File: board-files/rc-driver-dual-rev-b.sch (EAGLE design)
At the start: 20 parts

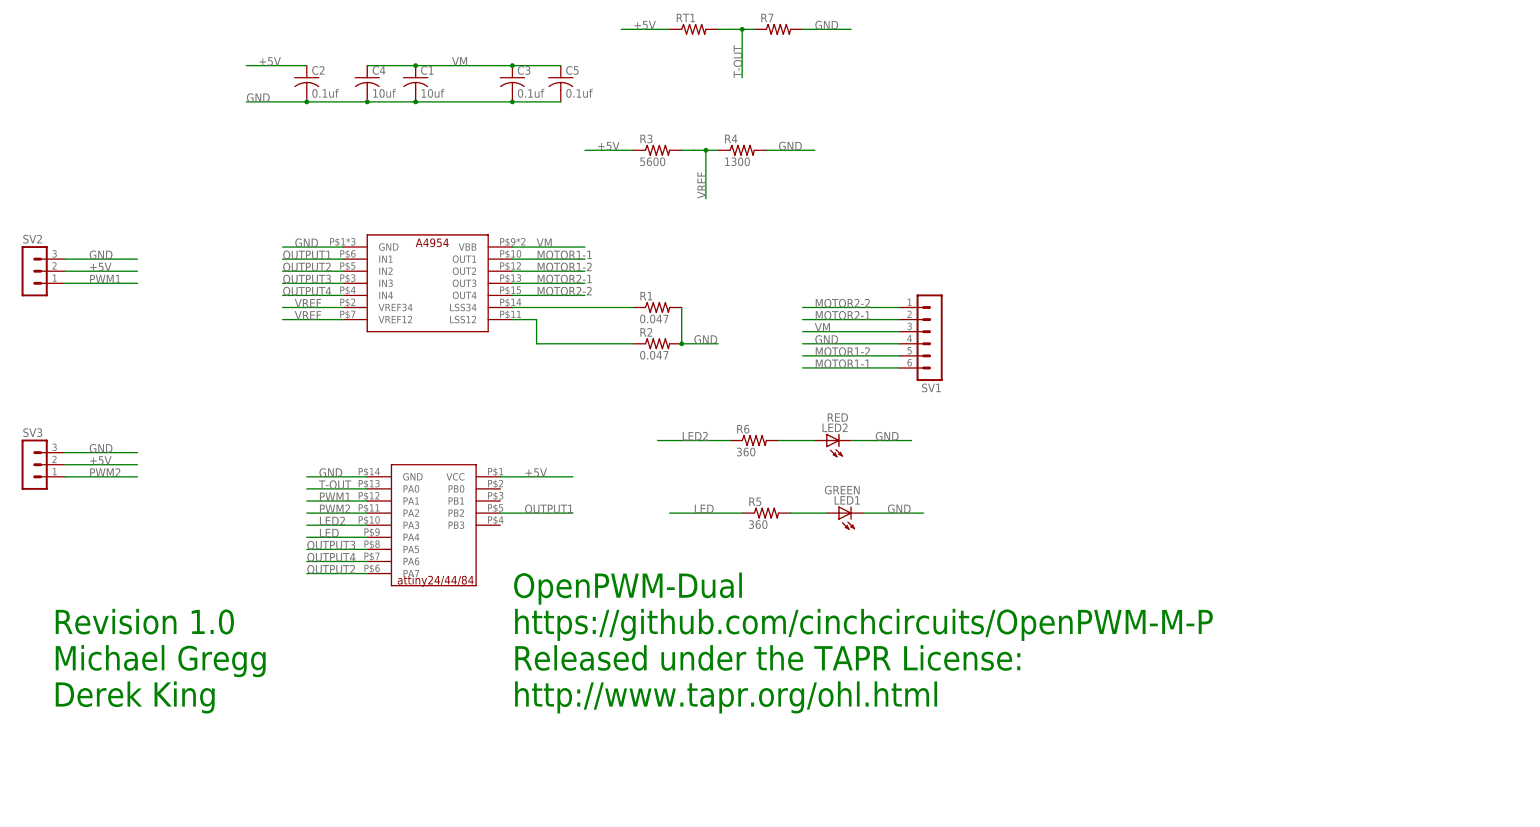
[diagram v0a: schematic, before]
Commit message: First pass layout of revB designed that include 5V regulator Improved part outlines in library.
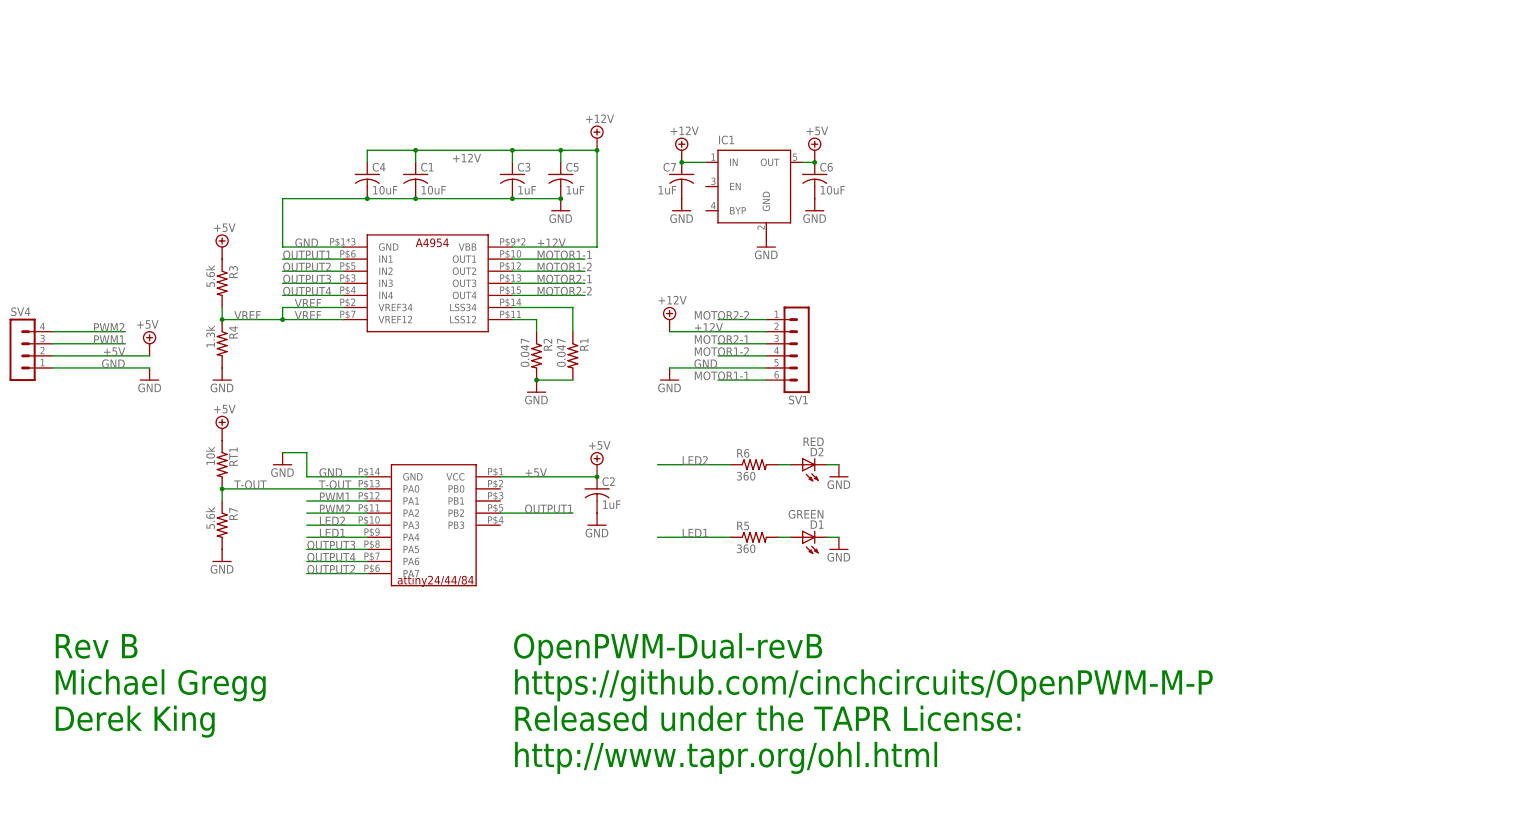
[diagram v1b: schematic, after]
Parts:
- removed LED1: GREEN, led:LEDCHIPLED_0603
- removed LED2: RED, led:LEDCHIPLED_0603
- removed SV2, SV3: (no value), con-lstb:MA03-1
- added C6: 10uF, resistor:C-USC1206
- added C7: 1uF, resistor:C-USC0603
- added D1: GREEN, led:LEDCHIPLED_0603
- added D2: RED, led:LEDCHIPLED_0603
- added IC1: (no value), v-reg-micrel:MIC5219XX
- added SV4: (no value), con-lstb:MA04-1
- C1, C4: value 10uf -> 10uF
- C2, C3, C5: value 0.1uf -> 1uF
- R1, R2: device resistor:R-US_R0805W -> resistor:R-US_R0805
- R3: value 5600 -> 5.6k
- R4: value 1300 -> 1.3k
- R7: value (none) -> 5.6k
- RT1: value (none) -> 10k
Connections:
- net LED renamed LED1
- removed net VM: C1.1, C3.1, C4.1, C5.1, SV1.3, U$2.VBB
- new net +12V: C1.1, C3.1, C4.1, C5.1, C7.1, IC1.IN, SV1.2, U$2.VBB
- net +5V: now also C6.1, IC1.OUT, SV4.2; no longer SV2.2, SV3.2
- net GND: now also C6.2, C7.2, D1.C, D2.C, IC1.GND, SV1.5, SV4.1; no longer LED1.C, LED2.C, SV1.4, SV2.3, SV3.3
- net MOTOR1-2: now also SV1.4; no longer SV1.5
- net MOTOR2-1: now also SV1.3; no longer SV1.2
- net N$3: now also D2.A; no longer LED2.A
- net N$4: now also D1.A; no longer LED1.A
- net PWM1: now also SV4.3; no longer SV2.1
- net PWM2: now also SV4.4; no longer SV3.1
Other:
- note added: "OpenPWM-Dual-revB"
- note added: "Rev B"
- note removed: "OpenPWM-Dual"
- note removed: "Revision 1.0"
- moved on the sheet: C1, C2, C3, C4, C5, R1, R2, R3, R4, R5, R6, R7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

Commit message: Added optional 6-DOF IMU to circuit board. Changed some parts to 0402.
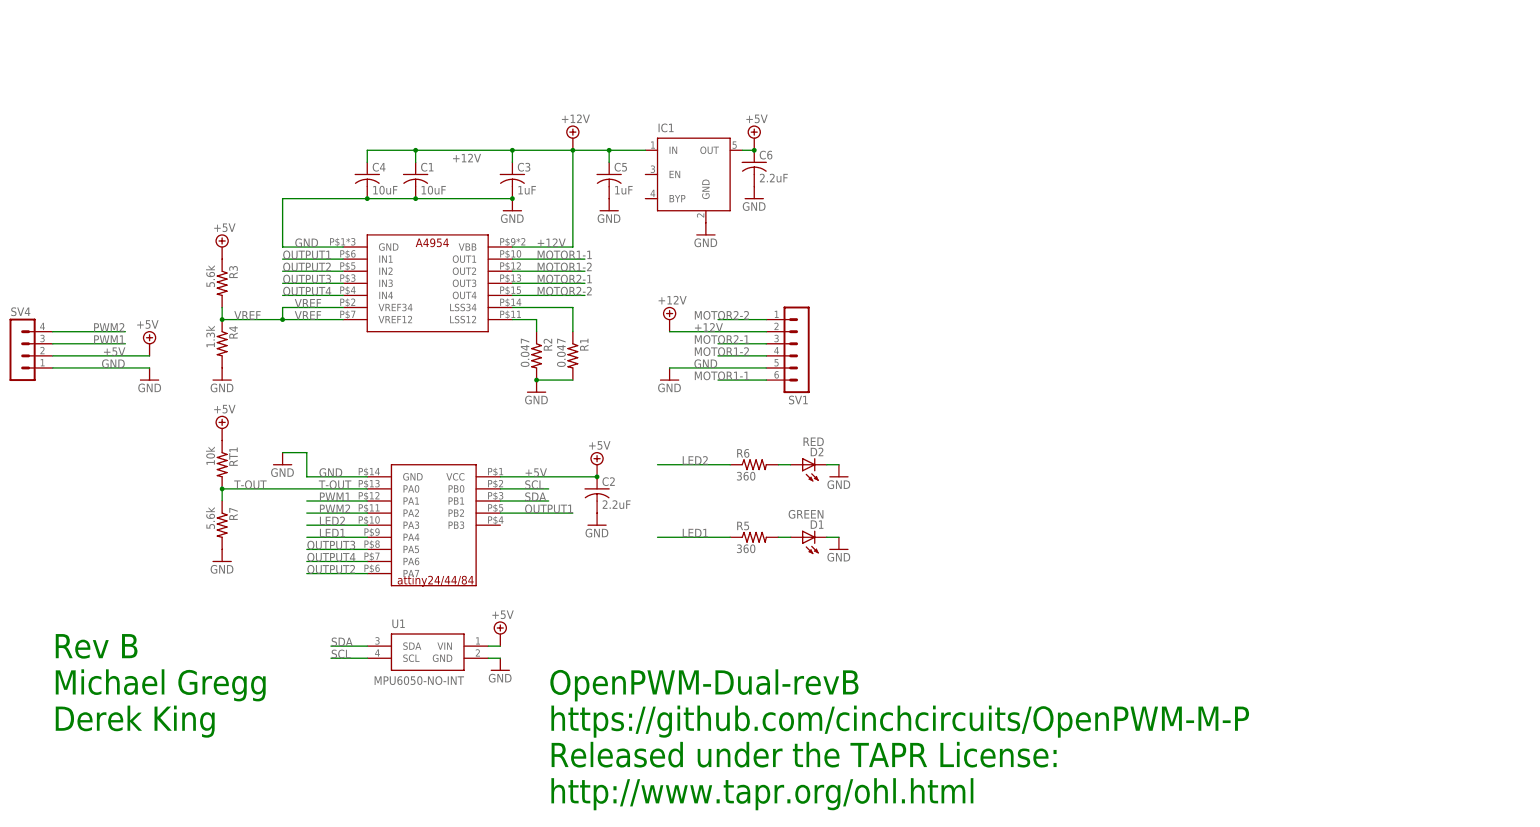
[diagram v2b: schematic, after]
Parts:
- removed C7: 1uF, resistor:C-USC0603
- added U1: MPU6050-NO-INT, rc-parts:MPU6050-NO-INT
- C2: value 1uF -> 2.2uF
- C6: value 10uF -> 2.2uF; device resistor:C-USC1206 -> resistor:C-USC0603
- R3, R4, R5, R6, R7, RT1: device resistor:R-US_R0603 -> resistor:R-US_R0402
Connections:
- new net SCL: U$1.PB0, U1.SCL
- new net SDA: U$1.PB1, U1.SDA
- net +12V: no longer C7.1
- net +5V: now also U1.VIN
- net GND: now also U1.GND; no longer C7.2
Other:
- moved on the sheet: C5, C6, IC1
